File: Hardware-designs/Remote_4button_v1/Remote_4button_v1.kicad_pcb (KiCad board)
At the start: 2 copper layers, 30 x 80 mm, 34 parts, among them J1 UART, J2 Bat, J3 USB_C, J4 Conn_01x08_Pin, SW1 PTS526 SM15 SMTR2 LFS, SW2 PTS526 SM15 SMTR2 LFS, SW3 PTS526 SM15 SMTR2 LFS, SW4 PTS526 SM15 SMTR2 LFS, SW5 PTS526 SM15 SMTR2 LFS, U1 ESP32-WROOM-32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

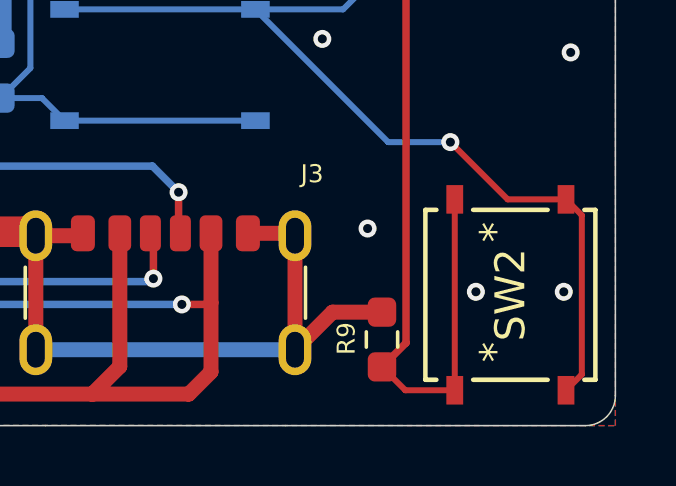
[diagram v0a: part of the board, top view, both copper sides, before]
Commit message: Add pcb images, step file, and pdf schematic for all hardware designs.
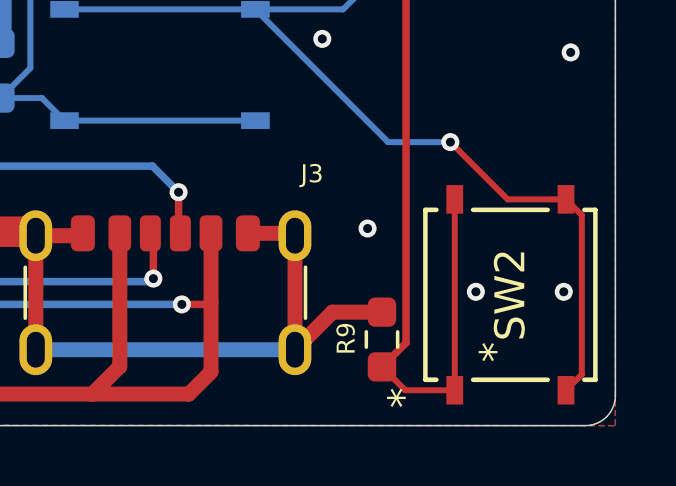
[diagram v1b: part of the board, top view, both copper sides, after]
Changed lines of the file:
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@@
 		)
 		(fp_text user "*"
-			(at 2.090349 -0.500001 90)
+			(at -3.43535 -3.556 90)
 			(layer "F.SilkS")
 			(effects
@@
 		)
 		(embedded_fonts no)
-		(model "/Users/gmixich/OneDrive/KiCad/esp_now_button_3.1/components/PTS526_SM15_SMTR2_LFS/PTS526SK15SMTR2_LFS.stp"
+		(model "${KIPRJMOD}/components/PTS526_SM15_SMTR2_LFS/PTS526SK15SMTR2_LFS.stp"
 			(offset
 				(xyz 0 0 0)
@@
 		(fp_text user "*"
 			(at -3.43535 3.556 180)
+			(unlocked yes)
 			(layer "B.SilkS")
 			(effects
@@
 		(fp_text user "*"
 			(at -3.43535 3.556 180)
-			(unlocked yes)
 			(layer "B.SilkS")
 			(effects
@@
 		)
 		(embedded_fonts no)
-		(model "/Users/gmixich/OneDrive/KiCad/esp_now_button_3.1/components/PTS526_SM15_SMTR2_LFS/PTS526SK15SMTR2_LFS.stp"
+		(model "${KIPRJMOD}/components/PTS526_SM15_SMTR2_LFS/PTS526SK15SMTR2_LFS.stp"
 			(offset
 				(xyz 0 0 0)
@@
 		(fp_text user "*"
 			(at -2.3241 2.6289 180)
-			(unlocked yes)
 			(layer "B.Fab")
 			(effects
@@
 			)
 		)
-		(fp_text user "*"
-			(at -2.3241 2.6289 180)
+		(fp_text user "${REFERENCE}"
+			(at 0 0 180)
+			(unlocked yes)
 			(layer "B.Fab")
 			(effects
@@
 			)
 		)
-		(fp_text user "${REFERENCE}"
-			(at 0 0 180)
+		(fp_text user "*"
+			(at -2.3241 2.6289 180)
 			(unlocked yes)
 			(layer "B.Fab")
@@
 		)
 		(embedded_fonts no)
-		(model "/Users/gmixich/OneDrive/KiCad/esp_now_button_3.1/components/PTS526_SM15_SMTR2_LFS/PTS526SK15SMTR2_LFS.stp"
+		(model "${KIPRJMOD}/components/PTS526_SM15_SMTR2_LFS/PTS526SK15SMTR2_LFS.stp"
 			(offset
 				(xyz 0 0 0)
@@
 		)
 		(embedded_fonts no)
-		(model "/Users/gmixich/OneDrive/KiCad/esp_now_button_3.1/components/PTS526_SM15_SMTR2_LFS/PTS526SK15SMTR2_LFS.stp"
+		(model "${KIPRJMOD}/components/PTS526_SM15_SMTR2_LFS/PTS526SK15SMTR2_LFS.stp"
 			(offset
 				(xyz 0 0 0)
@@
 		(fp_text user "*"
 			(at -3.43535 3.556 180)
-			(unlocked yes)
 			(layer "B.SilkS")
 			(effects
@@
 		(fp_text user "*"
 			(at -2.3241 2.6289 180)
+			(unlocked yes)
 			(layer "B.Fab")
 			(effects
@@
 		)
 		(embedded_fonts no)
-		(model "/Users/gmixich/OneDrive/KiCad/esp_now_button_3.1/components/PTS526_SM15_SMTR2_LFS/PTS526SK15SMTR2_LFS.stp"
+		(model "${KIPRJMOD}/components/PTS526_SM15_SMTR2_LFS/PTS526SK15SMTR2_LFS.stp"
 			(offset
 				(xyz 0 0 0)

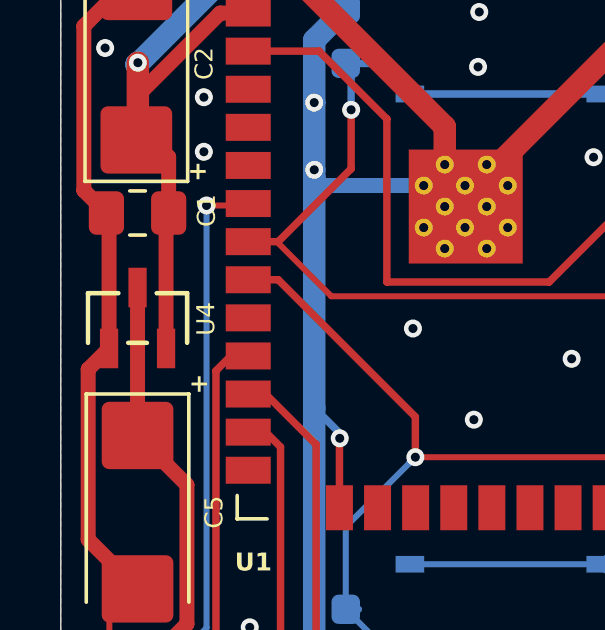
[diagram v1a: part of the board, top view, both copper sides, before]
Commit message: correction voltage regulator
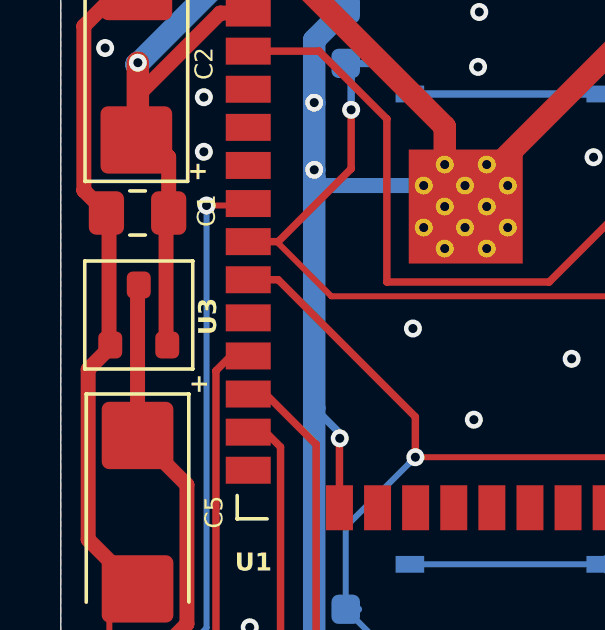
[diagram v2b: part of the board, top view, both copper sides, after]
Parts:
- removed U4: MCP1700, MCP1700T_3302E_TT 3:SOT-23_MC_MCH
- added U3: MCP1700T-1202E-TT, PCM_Package_TO_SOT_SMD_AKL:SOT-23, F.Cu at (102.6, 69.0)
- R14: value 270k -> 300

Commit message: Minor KiCad files update for all devices
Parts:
- C3: value 1nF -> 68nF
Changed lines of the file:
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@@
 			)
 		)
-		(property "Value" "1nF"
+		(property "Value" "68nF"
 			(at 0 1.68 0)
 			(layer "F.Fab")
